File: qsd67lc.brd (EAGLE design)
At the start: 160 x 100 mm, 43 parts, among them IC1 MEGA8-P, IC2 BTS555E3146, IC3 MAX3232CPE, IC4 LM2576S, T1 BCR141, U1 HC_05, X2 RS232

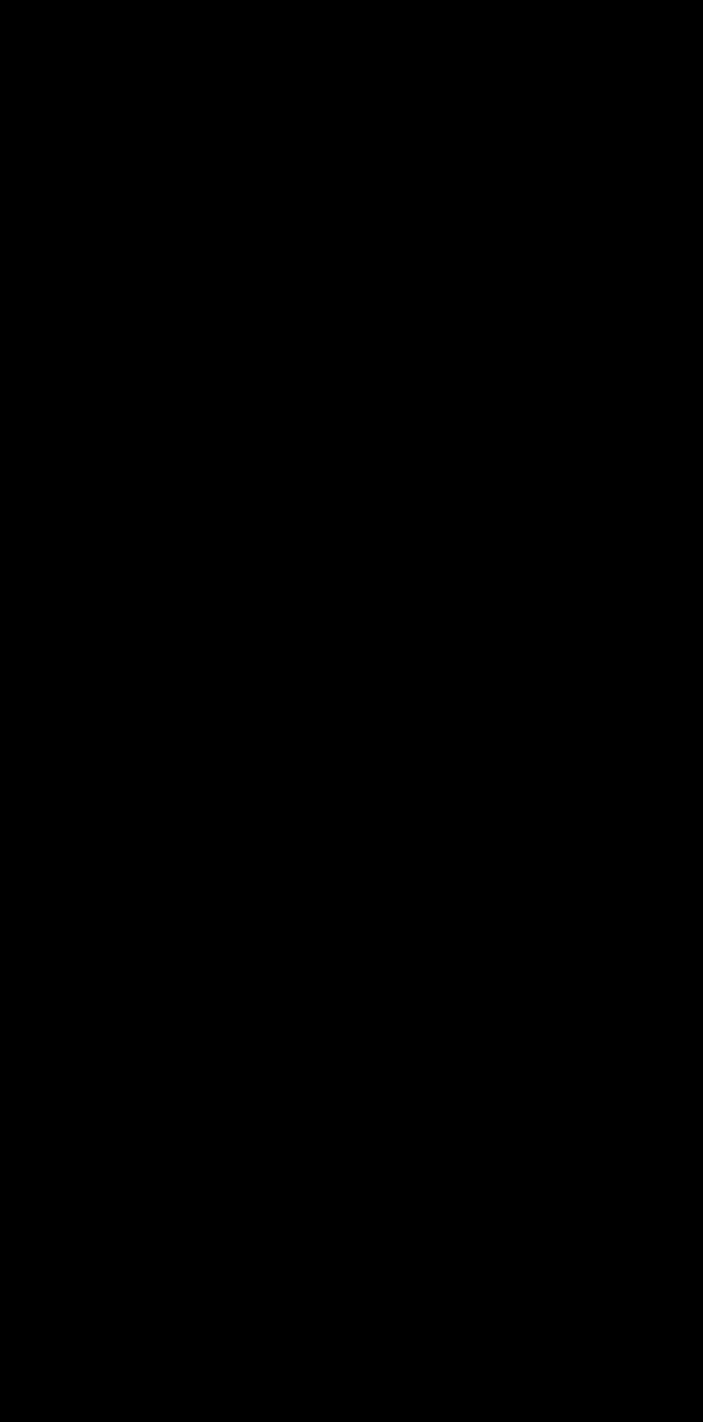
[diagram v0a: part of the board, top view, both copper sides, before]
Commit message: added connectors fixed rs232 dsub9 pinning added current supply circuit
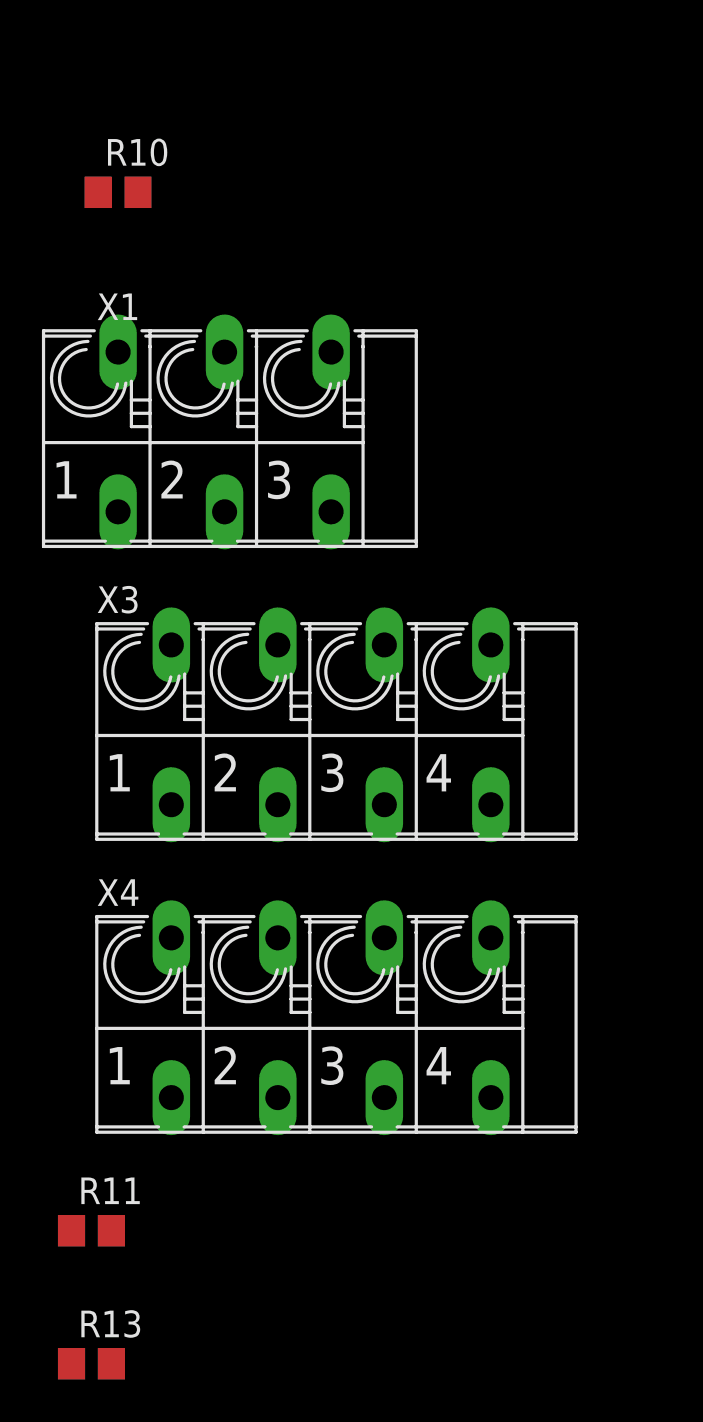
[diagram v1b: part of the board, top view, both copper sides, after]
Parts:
- added R10, R11, R13: 10k, rcl:R0805
- added X1: FFKV3, con-phoenix-508:FFKV3
- added X3, X4: FFKV4, con-phoenix-508:FFKV4
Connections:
- removed net IGN_OUT: IC2.1, IC2.5
- new net 12V_OUT: IC2.1, IC2.5, X4.4A
- new net IGN0_IN: R13.2, X3.1A
- new net IGN0_OUT: X4.1A
- new net IGN1_IN: X3.2A
- new net IGN1_OUT: X4.2A
- new net IGN2_IN: X3.3A
- new net IGN2_OUT: X4.3A
- new net QS+: IC1.4, R10.1, X1.2A
- new net QS-: X1.1A
- net +12V: now also X3.4A
- net +3V3: now also R10.2
- net GND: now also R11.1, X1.3A
- net RPM_INT: now also R11.2, R13.1
- net RS232_RX: now also X2.3; no longer X2.2
- net RS232_TX: now also X2.2; no longer X2.3
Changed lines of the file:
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@@
 <attribute name="VALUE" x="-102.87" y="-162.56" size="1.778" layer="27" ratio="10"/>
+</element>
+<element name="R10" library="rcl" library_urn="urn:adsk.eagle:library:334" package="R0805" package3d_urn="urn:adsk.eagle:package:23553/2" value="10k" x="-111.76" y="-201.93">
+<attribute name="NAME" x="-112.395" y="-200.66" size="1.27" layer="25"/>
+<attribute name="SPICEPREFIX" value="R" x="-111.76" y="-201.93" size="1.778" layer="27" display="off"/>
+<attribute name="VALUE" x="-112.395" y="-204.47" size="1.27" layer="27"/>
+</element>
+<element name="X1" library="con-phoenix-508" library_urn="urn:adsk.eagle:library:176" package="FFKV3" package3d_urn="urn:adsk.eagle:package:9576/1" value="FFKV3" x="-106.68" y="-213.36">
+<attribute name="MF" value="" x="-106.68" y="-213.36" size="1.778" layer="27" display="off"/>
+<attribute name="MPN" value="" x="-106.68" y="-213.36" size="1.778" layer="27" display="off"/>
+<attribute name="NAME" x="-112.776" y="-208.026" size="1.27" layer="25" ratio="10"/>
+<attribute name="OC_FARNELL" value="unknown" x="-106.68" y="-213.36" size="1.778" layer="27" display="off"/>
+<attribute name="OC_NEWARK" value="unknown" x="-106.68" y="-213.36" size="1.778" layer="27" display="off"/>
+<attribute name="VALUE" x="-100.711" y="-217.805" size="1.27" layer="27" ratio="10" rot="R90"/>
+</element>
+<element name="X3" library="con-phoenix-508" library_urn="urn:adsk.eagle:library:176" package="FFKV4" package3d_urn="urn:adsk.eagle:package:9586/1" value="FFKV4" x="-101.6" y="-227.33">
+<attribute name="MF" value="" x="-101.6" y="-227.33" size="1.778" layer="27" display="off"/>
+<attribute name="MPN" value="" x="-101.6" y="-227.33" size="1.778" layer="27" display="off"/>
+<attribute name="NAME" x="-112.776" y="-221.996" size="1.27" layer="25" ratio="10"/>
+<attribute name="OC_FARNELL" value="unknown" x="-101.6" y="-227.33" size="1.778" layer="27" display="off"/>
+<attribute name="OC_NEWARK" value="unknown" x="-101.6" y="-227.33" size="1.778" layer="27" display="off"/>
+<attribute name="VALUE" x="-90.551" y="-231.902" size="1.27" layer="27" ratio="10" rot="R90"/>
+</element>
+<element name="X4" library="con-phoenix-508" library_urn="urn:adsk.eagle:library:176" package="FFKV4" package3d_urn="urn:adsk.eagle:package:9586/1" value="FFKV4" x="-101.6" y="-241.3">
+<attribute name="MF" value="" x="-101.6" y="-241.3" size="1.778" layer="27" display="off"/>
+<attribute name="MPN" value="" x="-101.6" y="-241.3" size="1.778" layer="27" display="off"/>
+<attribute name="NAME" x="-112.776" y="-235.966" size="1.27" layer="25" ratio="10"/>
+<attribute name="OC_FARNELL" value="unknown" x="-101.6" y="-241.3" size="1.778" layer="27" display="off"/>
+<attribute name="OC_NEWARK" value="unknown" x="-101.6" y="-241.3" size="1.778" layer="27" display="off"/>
+<attribute name="VALUE" x="-90.551" y="-245.872" size="1.27" layer="27" ratio="10" rot="R90"/>
+</element>
+<element name="R11" library="rcl" library_urn="urn:adsk.eagle:library:334" package="R0805" package3d_urn="urn:adsk.eagle:package:23553/2" value="10k" x="-113.03" y="-251.46">
+<attribute name="NAME" x="-113.665" y="-250.19" size="1.27" layer="25"/>
+<attribute name="SPICEPREFIX" value="R" x="-113.03" y="-251.46" size="1.778" layer="27" display="off"/>
+<attribute name="VALUE" x="-113.665" y="-254" size="1.27" layer="27"/>
+</element>
+<element name="R13" library="rcl" library_urn="urn:adsk.eagle:library:334" package="R0805" package3d_urn="urn:adsk.eagle:package:23553/2" value="10k" x="-113.03" y="-257.81">
+<attribute name="NAME" x="-113.665" y="-256.54" size="1.27" layer="25"/>
+<attribute name="SPICEPREFIX" value="R" x="-113.03" y="-257.81" size="1.778" layer="27" display="off"/>
+<attribute name="VALUE" x="-113.665" y="-260.35" size="1.27" layer="27"/>
 </element>
 </elements>
@@
 <contactref element="X2" pad="5"/>
 <contactref element="X2" pad="1"/>
+<contactref element="X1" pad="3A"/>
+<contactref element="R11" pad="1"/>
 <wire x1="-95.25" y1="-137.16" x2="-105.41" y2="-146.05" width="0" layer="19" extent="1-1"/>
 <wire x1="-104.14" y1="-124.46" x2="-95.25" y2="-137.16" width="0" layer="19" extent="1-1"/>
@@
 <wire x1="-103.2764" y1="-177.8" x2="-105.41" y2="-146.05" width="0" layer="19" extent="1-1"/>
 <wire x1="-92.3036" y1="-177.8" x2="-103.2764" y2="-177.8" width="0" layer="19" extent="1-1"/>
+<wire x1="-101.6" y1="-209.55" x2="-103.2764" y2="-177.8" width="0" layer="19" extent="1-1"/>
 <wire x1="-96.52" y1="-73.66" x2="-94.25" y2="-107.78" width="0" layer="19" extent="1-1"/>
 <wire x1="-93.98" y1="-67.31" x2="-96.52" y2="-73.66" width="0" layer="19" extent="1-1"/>
@@
 <wire x1="-46.67" y1="67.31" x2="-39.69" y2="67.31" width="0" layer="19" extent="1-1"/>
 <wire x1="-51.75" y1="67.31" x2="-46.67" y2="67.31" width="0" layer="19" extent="1-1"/>
+<wire x1="-113.98" y1="-251.46" x2="-101.6" y2="-209.55" width="0" layer="19" extent="1-1"/>
 </signal>
 <signal name="RXD">
@@
 <contactref element="C10" pad="+"/>
 <contactref element="IC4" pad="4"/>
+<contactref element="R10" pad="2"/>
 <wire x1="-110.49" y1="-146.05" x2="-97.79" y2="-156.21" width="0" layer="19" extent="1-1"/>
 <wire x1="-104.9782" y1="-115.0112" x2="-110.49" y2="-146.05" width="0" layer="19" extent="1-1"/>
+<wire x1="-110.81" y1="-201.93" x2="-97.79" y2="-156.21" width="0" layer="19" extent="1-1"/>
 <wire x1="-93.98" y1="-41.91" x2="-104.9782" y2="-115.0112" width="0" layer="19" extent="1-1"/>
 <wire x1="-96.2" y1="-36.83" x2="-93.98" y2="-41.91" width="0" layer="19" extent="1-1"/>
@@
 <signal name="RPM_INT">
 <contactref element="IC1" pad="5"/>
+<contactref element="R13" pad="1"/>
+<contactref element="R11" pad="2"/>
+<wire x1="-112.08" y1="-251.46" x2="-113.98" y2="-257.81" width="0" layer="19" extent="1-1"/>
+<wire x1="-38.1" y1="33.02" x2="-112.08" y2="-251.46" width="0" layer="19" extent="1-1"/>
 </signal>
 <signal name="MODE_KEY">
@@
 <wire x1="-17.78" y1="33.02" x2="-96.25" y2="-107.78" width="0" layer="19" extent="1-1"/>
 </signal>
-<signal name="IGN_OUT">
+<signal name="12V_OUT">
 <contactref element="IC2" pad="1"/>
 <contactref element="IC2" pad="5"/>
+<contactref element="X4" pad="4A"/>
 <wire x1="-64.77" y1="-21.59" x2="-74.93" y2="-21.59" width="0" layer="19" extent="1-1"/>
+<wire x1="-93.98" y1="-237.49" x2="-74.93" y2="-21.59" width="0" layer="19" extent="1-1"/>
 </signal>
 <signal name="+12V">
@@
 <contactref element="C9" pad="+"/>
 <contactref element="IC4" pad="1"/>
+<contactref element="X3" pad="4A"/>
 <wire x1="-110.0836" y1="-115.0112" x2="-109.22" y2="-124.46" width="0" layer="19" extent="1-1"/>
 <wire x1="-94.3" y1="-114.3" x2="-110.0836" y2="-115.0112" width="0" layer="19" extent="1-1"/>
 <wire x1="-69.85" y1="-21.59" x2="-94.3" y2="-114.3" width="0" layer="19" extent="1-1"/>
+<wire x1="-93.98" y1="-223.52" x2="-109.22" y2="-124.46" width="0" layer="19" extent="1-1"/>
 </signal>
 <signal name="TXD_BT">
@@
 <signal name="RS232_RX">
 <contactref element="IC3" pad="14"/>
-<contactref element="X2" pad="2"/>
-<wire x1="-100.5332" y1="-177.8" x2="-88.9" y2="-41.91" width="0" layer="19" extent="1-1"/>
+<contactref element="X2" pad="3"/>
+<wire x1="-97.79" y1="-177.8" x2="-88.9" y2="-41.91" width="0" layer="19" extent="1-1"/>
 </signal>
 <signal name="RS232_TX">
 <contactref element="IC3" pad="13"/>
-<contactref element="X2" pad="3"/>
-<wire x1="-97.79" y1="-177.8" x2="-86.36" y2="-41.91" width="0" layer="19" extent="1-1"/>
+<contactref element="X2" pad="2"/>
+<wire x1="-100.5332" y1="-177.8" x2="-86.36" y2="-41.91" width="0" layer="19" extent="1-1"/>
 </signal>
 <signal name="N$16">
@@
 <wire x1="-108.3818" y1="-115.0112" x2="-110.49" y2="-137.16" width="0" layer="19" extent="1-1"/>
 </signal>
+<signal name="QS+">
+<contactref element="R10" pad="1"/>
+<contactref element="IC1" pad="4"/>
+<contactref element="X1" pad="2A"/>
+<wire x1="-106.68" y1="-209.55" x2="-112.71" y2="-201.93" width="0" layer="19" extent="1-1"/>
+<wire x1="-40.64" y1="33.02" x2="-112.71" y2="-201.93" width="0" layer="19" extent="1-1"/>
+</signal>
+<signal name="QS-">
+<contactref element="X1" pad="1A"/>
+</signal>
+<signal name="IGN2_OUT">
+<contactref element="X4" pad="3A"/>
+</signal>
+<signal name="IGN1_OUT">
+<contactref element="X4" pad="2A"/>
+</signal>
+<signal name="IGN0_OUT">
+<contactref element="X4" pad="1A"/>
+</signal>
+<signal name="IGN2_IN">
+<contactref element="X3" pad="3A"/>
+</signal>
+<signal name="IGN1_IN">
+<contactref element="X3" pad="2A"/>
+</signal>
+<signal name="IGN0_IN">
+<contactref element="X3" pad="1A"/>
+<contactref element="R13" pad="2"/>
+<wire x1="-109.22" y1="-223.52" x2="-112.08" y2="-257.81" width="0" layer="19" extent="1-1"/>
+</signal>
 </signals>
